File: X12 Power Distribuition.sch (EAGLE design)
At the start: 38 parts, among them Q1 SPB80P06P, Y1 ECS-80-S-4X

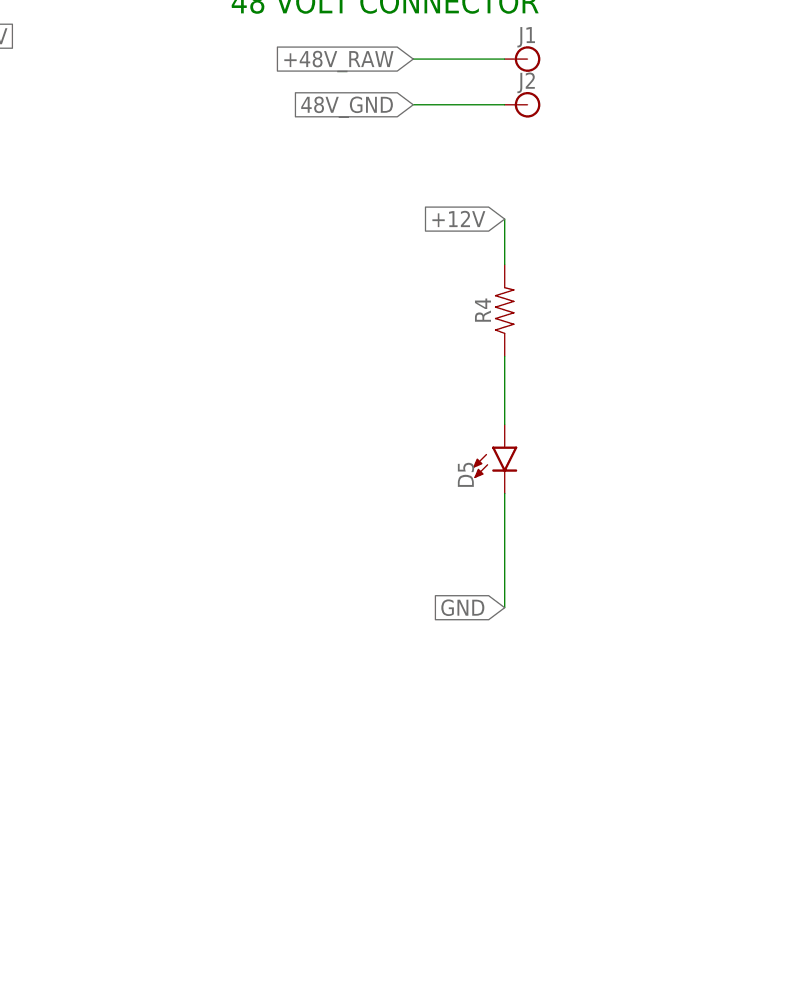
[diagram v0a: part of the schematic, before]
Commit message: Added POE through holes
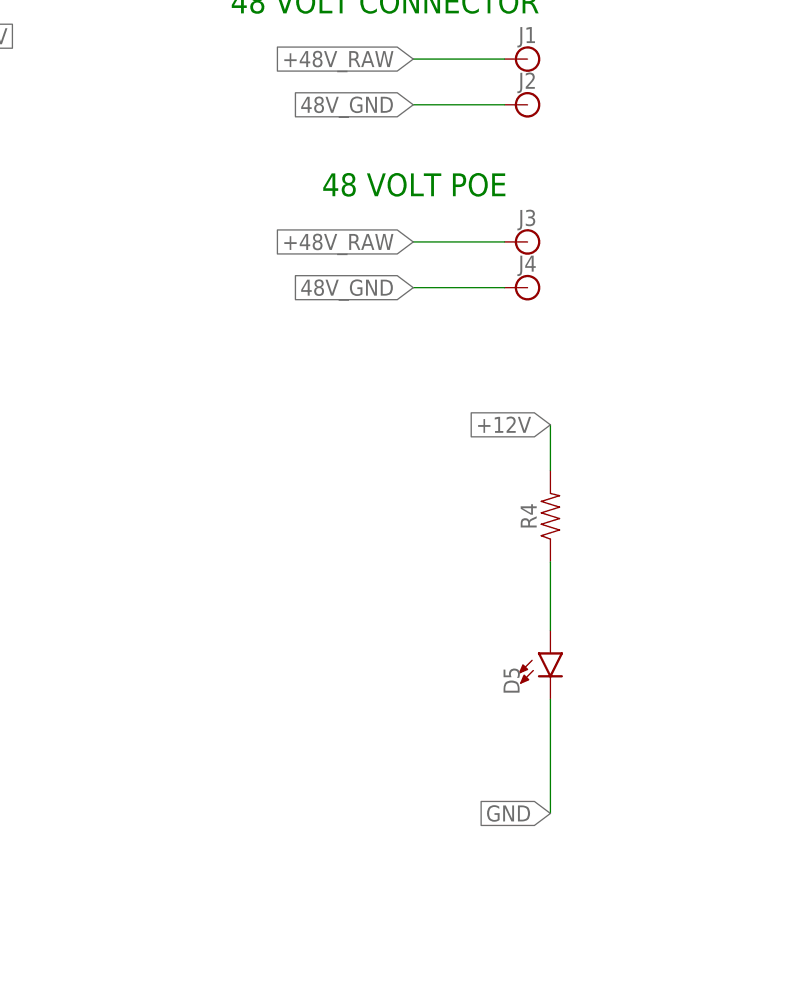
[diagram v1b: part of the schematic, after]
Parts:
- added J3, J4: (no value), SparkFun-Connectors:BANANA_CONN
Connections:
- net +48V_RAW: now also J3.1
- net 48V_GND: now also J4.1
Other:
- note added: "48 VOLT POE"
- moved on the sheet: D5, R4
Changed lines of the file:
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@@
 <part name="GND11" library="supply2" library_urn="urn:adsk.eagle:library:372" deviceset="GND" device=""/>
 <part name="FRAME2" library="SparkFun-Aesthetics" library_urn="urn:adsk.eagle:library:507" deviceset="FRAME-A4L" device=""/>
+<part name="J3" library="SparkFun-Connectors" deviceset="BANANA_CONN" device=""/>
+<part name="J4" library="SparkFun-Connectors" deviceset="BANANA_CONN" device=""/>
 </parts>
 <sheets>
@@
 <text x="449.58" y="55.88" size="1.778" layer="91">Pin 17 (VDDIO2)</text>
 <text x="477.52" y="55.88" size="1.778" layer="91">Pin 5 (VDDA)</text>
+<text x="218.44" y="139.7" size="2.54" layer="91">48 VOLT POE</text>
 </plain>
 <instances>
@@
 <attribute name="NAME" x="143.51" y="151.13" size="1.778" layer="95"/>
 </instance>
-<instance part="D5" gate="G$1" x="238.76" y="111.76" smashed="yes">
-<attribute name="NAME" x="235.331" y="107.188" size="1.778" layer="95" font="vector" rot="R90"/>
-<attribute name="VALUE" x="240.665" y="107.188" size="1.778" layer="96" font="vector" rot="R90" align="top-left"/>
-</instance>
-<instance part="R4" gate="G$1" x="238.76" y="127" smashed="yes" rot="R90">
-<attribute name="NAME" x="237.236" y="127" size="1.778" layer="95" font="vector" rot="R90" align="bottom-center"/>
-<attribute name="VALUE" x="240.284" y="127" size="1.778" layer="96" font="vector" rot="R90" align="top-center"/>
+<instance part="D5" gate="G$1" x="243.84" y="88.9" smashed="yes">
+<attribute name="NAME" x="240.411" y="84.328" size="1.778" layer="95" font="vector" rot="R90"/>
+<attribute name="VALUE" x="245.745" y="84.328" size="1.778" layer="96" font="vector" rot="R90" align="top-left"/>
+</instance>
+<instance part="R4" gate="G$1" x="243.84" y="104.14" smashed="yes" rot="R90">
+<attribute name="NAME" x="242.316" y="104.14" size="1.778" layer="95" font="vector" rot="R90" align="bottom-center"/>
+<attribute name="VALUE" x="245.364" y="104.14" size="1.778" layer="96" font="vector" rot="R90" align="top-center"/>
 </instance>
 <instance part="J1" gate="G$1" x="241.3" y="154.94" smashed="yes">
@@
 <attribute name="LAST_DATE_TIME" x="486.41" y="6.35" size="2.286" layer="94" font="vector"/>
 <attribute name="SHEET" x="500.38" y="1.27" size="2.54" layer="94" font="vector"/>
+</instance>
+<instance part="J3" gate="G$1" x="241.3" y="134.62" smashed="yes">
+<attribute name="NAME" x="240.284" y="136.398" size="1.778" layer="95" font="vector"/>
+<attribute name="VALUE" x="240.284" y="131.572" size="1.778" layer="96" font="vector"/>
+</instance>
+<instance part="J4" gate="G$1" x="241.3" y="129.54" smashed="yes">
+<attribute name="NAME" x="240.284" y="131.318" size="1.778" layer="95" font="vector"/>
+<attribute name="VALUE" x="240.284" y="126.492" size="1.778" layer="96" font="vector"/>
 </instance>
 </instances>
@@
 <segment>
 <pinref part="R4" gate="G$1" pin="2"/>
-<wire x1="238.76" y1="132.08" x2="238.76" y2="137.16" width="0.1524" layer="91"/>
-<label x="238.76" y="137.16" size="1.778" layer="95" rot="R180" xref="yes"/>
+<wire x1="243.84" y1="109.22" x2="243.84" y2="114.3" width="0.1524" layer="91"/>
+<label x="243.84" y="114.3" size="1.778" layer="95" rot="R180" xref="yes"/>
 </segment>
 </net>
@@
 <label x="93.98" y="109.22" size="1.778" layer="95" rot="R270" xref="yes"/>
 </segment>
+<segment>
+<pinref part="J4" gate="G$1" pin="1"/>
+<wire x1="238.76" y1="129.54" x2="228.6" y2="129.54" width="0.1524" layer="91"/>
+<label x="228.6" y="129.54" size="1.778" layer="95" rot="R180" xref="yes"/>
+</segment>
 </net>
 <net name="+48V_RAW" class="0">
@@
 <label x="228.6" y="154.94" size="1.778" layer="95" rot="R180" xref="yes"/>
 </segment>
+<segment>
+<pinref part="J3" gate="G$1" pin="1"/>
+<wire x1="238.76" y1="134.62" x2="228.6" y2="134.62" width="0.1524" layer="91"/>
+<label x="228.6" y="134.62" size="1.778" layer="95" rot="R180" xref="yes"/>
+</segment>
 </net>
 <net name="GND" class="0">
 <segment>
 <pinref part="D5" gate="G$1" pin="C"/>
-<wire x1="238.76" y1="93.98" x2="238.76" y2="106.68" width="0.1524" layer="91"/>
-<label x="238.76" y="93.98" size="1.778" layer="95" rot="R180" xref="yes"/>
+<wire x1="243.84" y1="71.12" x2="243.84" y2="83.82" width="0.1524" layer="91"/>
+<label x="243.84" y="71.12" size="1.778" layer="95" rot="R180" xref="yes"/>
 </segment>
 <segment>
@@
 <pinref part="D5" gate="G$1" pin="A"/>
 <pinref part="R4" gate="G$1" pin="1"/>
-<wire x1="238.76" y1="114.3" x2="238.76" y2="121.92" width="0.1524" layer="91"/>
-</segment>
-</net>
+<wire x1="243.84" y1="91.44" x2="243.84" y2="99.06" width="0.1524" layer="91"/>
+</segment>
+</net>
